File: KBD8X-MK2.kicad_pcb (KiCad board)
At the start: 2 copper layers, 343.7 x 118.3 mm, 347 parts, among them J1 AVR-ISP-6, Q1 DSS60601MZ4-13, SW1 SW_Push, SW2 SW_SPDT, SW3 SW_SPDT, U1 ATmega32U4-MU, U2 PRTR5V0U2X, Y1 16MHz

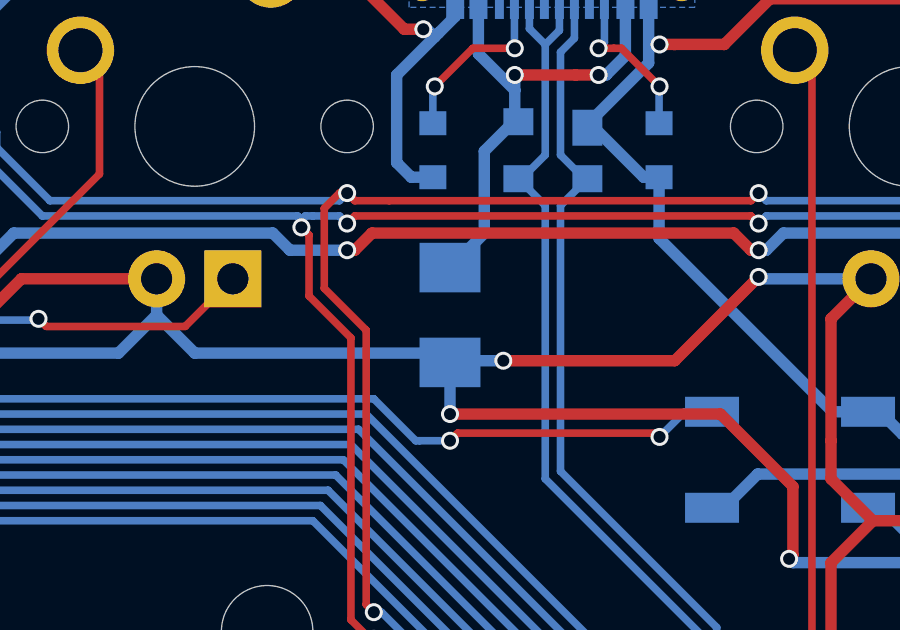
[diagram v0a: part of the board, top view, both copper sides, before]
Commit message: Made the project portable
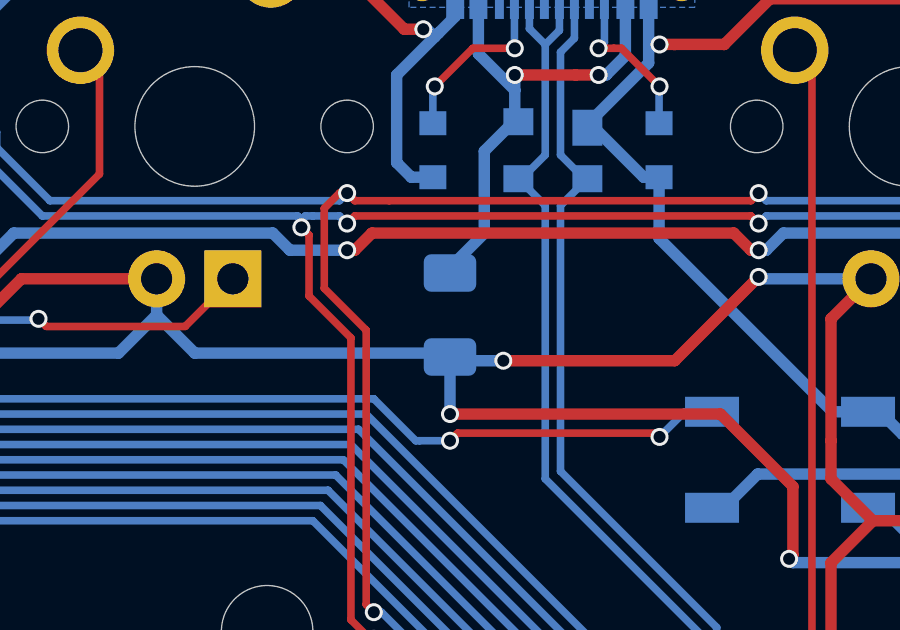
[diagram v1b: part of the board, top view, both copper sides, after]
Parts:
- C2, C3, C4, C5, C6, C7, C8, CRGB1, CRGB10, CRGB11, CRGB12, CRGB13, CRGB14, CRGB15, CRGB16, CRGB17, CRGB18, CRGB2, CRGB3, CRGB4, CRGB5, CRGB6, CRGB7, CRGB8, CRGB9: footprint locallib:C_0603 -> KBD8X_MK2_Components:C_0603
- D1, D10, D100, D101, D108, D11, D111, D112, D113, D12, D13, D14, D17, D18, D19, D2, D20, D21, D22, D23, D24, D25, D26, D27, D28, D29, D3, D30, D31, D35, D36, D37, D38, D39, D4, D40, D41, D42, D43, D44, D45, D46, D47, D48, D5, D52, D53, D54, D55, D56, D57, D58, D59, D6, D60, D61, D62, D63, D65, D66, D67, D68, D69, D7, D70, D71, D72, D73, D74, D75, D76, D77, D78, D8, D81, D82, D84, D85, D86, D87, D9, D90, D91, D92, D93, D94, D95, D96, D97, D99: footprint locallib:D_SOD-123 -> KBD8X_MK2_Components:D_SOD-123
- F1: footprint Fuse_Holders_and_Fuses:Fuse_SMD1206_Wave -> KBD8X_MK2_Components:Fuse_1206_3216Metric
- G***: footprint locallib:kbd8x-logo -> KBD8X_MK2_Graphics:kbd8x-logo
- G***: footprint locallib:ai-ring-6mm -> KBD8X_MK2_Graphics:ai-ring-6mm
- G***: footprint locallib:ai-ring-6mm-FancyAss-Mask -> KBD8X_MK2_Graphics:ai-ring-6mm-FancyAss-Mask
- G***: footprint locallib:ai-ring-6mm-FancyAss -> KBD8X_MK2_Graphics:ai-ring-6mm-FancyAss
- J1: footprint random-keyboard-parts:Reset_Pretty-Mask -> KBD8X_MK2_Components:Reset_Pretty-Mask
- MX_#0_1, MX_#1, MX_#2, MX_#3, MX_#4, MX_#5, MX_#6, MX_#7, MX_#8, MX_#9, MX_'1, MX_,1, MX_-1, MX_.1, MX_/1, MX_;1, MX_=1, MX_A1, MX_B1, MX_BACK2, MX_BACK3, MX_C1, MX_D1, MX_DEL1, MX_DN1, MX_E1, MX_END1, MX_ESC1, MX_F1, MX_FN1, MX_FN10, MX_FN11, MX_FN12, MX_FN2, MX_FN3, MX_FN4, MX_FN5, MX_FN6, MX_FN7, MX_FN8, MX_FN9, MX_G1, MX_H1, MX_HOME1, MX_I1, MX_INS1, MX_J1, MX_K1, MX_L1, MX_LFT1, MX_LSHIFT3, MX_M1, MX_N1, MX_O1, MX_P1, MX_PAUSE1, MX_PGDN1, MX_PGUP1, MX_PRINT1, MX_Q1, MX_R1, MX_RGUI2, MX_RSHIFT3, MX_RT1, MX_S1, MX_SLOCK1, MX_T1, MX_U1, MX_UP1, MX_V1, MX_W1, MX_X1, MX_Y1, MX_Z1, MX_[1, MX_\2, MX_]1, MX_`1: footprint MX_Alps_Hybrid:MXOnly-1U -> KBD8X_MK2_Switches:MXOnly-1U
- MX_BACK1: footprint MX_Alps_Hybrid:MXOnly-2U -> KBD8X_MK2_Switches:MXOnly-2U
- MX_CLOCK1, MX_RSHIFT2: footprint MX_Alps_Hybrid:MXOnly-1.75U -> KBD8X_MK2_Switches:MXOnly-1.75U
- MX_CLOCK2, MX_RCTRL1, MX_RGUI1, MX_RMENU1: footprint MX_Alps_Hybrid:MXOnly-1.25U-FLIPPED -> KBD8X_MK2_Switches:MXOnly-1.25U-FLIPPED
- MX_LALT1, MX_LCTRL1, MX_LGUI1, MX_LSHIFT2, MX_RALT1: footprint MX_Alps_Hybrid:MXOnly-1.25U -> KBD8X_MK2_Switches:MXOnly-1.25U
- MX_LALT2, MX_LCTRL2: footprint MX_Alps_Hybrid:MXOnly-1.5U-FLIPPED -> KBD8X_MK2_Switches:MXOnly-1.5U-FLIPPED
- MX_LGUI2: footprint MX_Alps_Hybrid:MXOnly-1U-FLIPPED -> KBD8X_MK2_Switches:MXOnly-1U-FLIPPED
- MX_LSHIFT1, MX_RETURN1: footprint MX_Alps_Hybrid:MXOnly-2.25U -> KBD8X_MK2_Switches:MXOnly-2.25U
- MX_RALT2, MX_RCTRL2, MX_TAB1, MX_\1: footprint MX_Alps_Hybrid:MXOnly-1.5U -> KBD8X_MK2_Switches:MXOnly-1.5U
- MX_RETURN2: footprint MX_Alps_Hybrid:MXOnly-ISO-ROTATED-ReversedStabilizers -> KBD8X_MK2_Switches:MXOnly-ISO-ROTATED-ReversedStabilizers
- MX_RSHIFT1: footprint MX_Alps_Hybrid:MXOnly-2.75U -> KBD8X_MK2_Switches:MXOnly-2.75U
- MX_SP1: footprint MX_Alps_Hybrid:MXOnly-6.25U-ReversedStabilizers -> KBD8X_MK2_Switches:MXOnly-6.25U-ReversedStabilizers
- MX_SP2: footprint MX_Alps_Hybrid:MXOnly-7U-ReversedStabilizers -> KBD8X_MK2_Switches:MXOnly-7U-ReversedStabilizers
- Q1: footprint TO_SOT_Packages_SMD:SOT-223-3_TabPin2 -> KBD8X_MK2_Components:SOT-223-3_TabPin2
- R1, R10, R100, R101, R108, R11, R111, R112, R113, R12, R13, R14, R16, R17, R18, R19, R2, R20, R21, R22, R23, R24, R25, R26, R27, R28, R29, R3, R30, R31, R32, R33, R35, R36, R37, R38, R39, R4, R40, R41, R42, R43, R44, R45, R46, R47, R48, R5, R52, R53, R54, R55, R56, R57, R58, R59, R6, R60, R61, R62, R63, R65, R66, R67, R68, R69, R7, R70, R71, R72, R73, R74, R75, R76, R77, R78, R8, R81, R82, R84, R85, R86, R87, R9, R90, R91, R95, R96, R97, R99, RC1, RC2, RC3, RC4, RC5, RC6, RC7: footprint locallib:R_0603 -> KBD8X_MK2_Components:R_0603
- RGB1, RGB10, RGB11, RGB12, RGB13, RGB14, RGB15, RGB16, RGB17, RGB18, RGB2, RGB3, RGB4, RGB5, RGB6, RGB7, RGB8, RGB9: footprint locallib:LED_WS2812B-PLCC4 -> KBD8X_MK2_Components:LED_WS2812B-PLCC4
- SW1: footprint random-keyboard-parts:SKQG-1155865 -> KBD8X_MK2_Components:SKQG-1155865
- SW2, SW3: footprint Buttons_Switches_SMD:SW_SPDT_PCM12 -> KBD8X_MK2_Components:SW_SPDT_PCM12
- U1: footprint locallib:QFN-44-1EP_7x7mm_Pitch0.5mm -> KBD8X_MK2_Components:QFN-44-1EP_7x7mm_Pitch0.5mm
- U2: footprint locallib:SOT143B -> KBD8X_MK2_Components:SOT143B
- USB1: footprint Type-C:HRO-TYPE-C-31-M-12-Assembly -> KBD8X_MK2_Components:HRO-TYPE-C-31-M-12-Assembly
- Y1: footprint locallib:Crystal_SMD_3225-4pin_3.2x2.5mm -> KBD8X_MK2_Components:Crystal_SMD_3225-4pin_3.2x2.5mm

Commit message: Rearrenged schematics items
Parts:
- removed G***: LOGO, KBD8X_MK2_Graphics:kbd8x-logo
- removed G***: LOGO, KBD8X_MK2_Graphics:ai-ring-6mm
- removed G***: LOGO, KBD8X_MK2_Graphics:ai-ring-6mm-FancyAss-Mask
- removed G***: LOGO, KBD8X_MK2_Graphics:ai-ring-6mm-FancyAss
- added H1: KBD8X-MKII Logo, KBD8X_MK2_Graphics:kbd8x-logo, F.Cu at (231.2, 252.9)
- added H2: ai03 logo, KBD8X_MK2_Graphics:ai-ring-6mm-FancyAss, B.Cu at (303.2, 252.4)
- added H3: ai03 logo, KBD8X_MK2_Graphics:ai-ring-6mm-FancyAss-Mask, B.Cu at (303.2, 252.4)
- added H4: ai03 logo, KBD8X_MK2_Graphics:ai-ring-6mm, F.Cu at (315.2, 253.2)
- D1, D10, D100, D101, D108, D11, D111, D112, D113, D12, D13, D14, D17, D18, D19, D2, D20, D21, D22, D23, D24, D25, D26, D27, D28, D29, D3, D30, D31, D35, D36, D37, D38, D39, D4, D40, D41, D42, D43, D44, D45, D46, D47, D48, D5, D52, D53, D54, D55, D56, D57, D58, D59, D6, D60, D61, D62, D63, D65, D66, D67, D68, D69, D7, D70, D71, D72, D73, D74, D75, D76, D77, D78, D8, D81, D82, D84, D85, D86, D87, D9, D90, D91, D92, D93, D94, D95, D96, D97, D99: value SOD-323 -> SOD-123
- RGB1, RGB10, RGB11, RGB12, RGB13, RGB14, RGB15, RGB16, RGB17, RGB18, RGB2, RGB3, RGB4, RGB5, RGB6, RGB7, RGB8, RGB9: footprint KBD8X_MK2_Components:LED_WS2812B-PLCC4 -> LED_SMD:LED_WS2812B_PLCC4_5.0x5.0mm_P3.2mm
- U1: footprint KBD8X_MK2_Components:QFN-44-1EP_7x7mm_Pitch0.5mm -> Package_DFN_QFN:QFN-44-1EP_7x7mm_P0.5mm_EP5.2x5.2mm
- moved CRGB10 144.0 mm to (146.1, 252.4)
- moved CRGB12 144.0 mm to (241.3, 252.4)
- moved CRGB13 144.0 mm to (281.8, 252.4)
- moved CRGB14 144.0 mm to (312.8, 252.4)
- moved CRGB16 144.0 mm to (412.8, 252.4)
- moved CRGB17 144.0 mm to (446.9, 254.8)
- moved D100 144.0 mm to (451.7, 196.9)
- moved D101 144.0 mm to (454.9, 196.9)
- moved D37 144.0 mm to (189.7, 196.9)
- moved D39 144.0 mm to (227.8, 196.9)
- moved D40 144.0 mm to (246.9, 196.9)
- moved D41 144.0 mm to (265.9, 196.9)
- moved D42 144.0 mm to (285.0, 196.9)
- moved D43 144.0 mm to (304.0, 196.9)
- moved D46 144.0 mm to (361.2, 196.9)
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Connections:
- RGB18 pad 2: Net-(RGB18-Pad2) -> unconnected-(RGB18-Pad2)
- SW1 pad 3: (no net) -> unconnected-(SW1-Pad3)
- SW1 pad 4: (no net) -> unconnected-(SW1-Pad4)
- U1 pad 42: Net-(U1-Pad42) -> unconnected-(U1-Pad42)
- USB1 pad 3: Net-(USB1-Pad3) -> unconnected-(USB1-Pad3)
- USB1 pad 9: Net-(USB1-Pad9) -> unconnected-(USB1-Pad9)
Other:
- outline, holes or cut-outs redrawn

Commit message: Updated symbols used in the schematics
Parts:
- MX_#0_1, MX_#1, MX_#2, MX_#3, MX_#4, MX_#5, MX_#6, MX_#7, MX_#8, MX_#9, MX_'1, MX_,1, MX_-1, MX_.1, MX_/1, MX_;1, MX_=1, MX_A1, MX_B1, MX_BACK2, MX_BACK3, MX_C1, MX_D1, MX_DEL1, MX_DN1, MX_E1, MX_END1, MX_ESC1, MX_F1, MX_FN1, MX_FN10, MX_FN11, MX_FN12, MX_FN2, MX_FN3, MX_FN4, MX_FN5, MX_FN6, MX_FN7, MX_FN8, MX_FN9, MX_G1, MX_H1, MX_HOME1, MX_I1, MX_INS1, MX_J1, MX_K1, MX_L1, MX_LFT1, MX_LGUI2, MX_LSHIFT3, MX_M1, MX_N1, MX_O1, MX_P1, MX_PAUSE1, MX_PGDN1, MX_PGUP1, MX_PRINT1, MX_Q1, MX_R1, MX_RGUI2, MX_RSHIFT3, MX_RT1, MX_S1, MX_SLOCK1, MX_T1, MX_U1, MX_UP1, MX_V1, MX_W1, MX_X1, MX_Y1, MX_Z1, MX_[1, MX_\2, MX_]1, MX_`1: value MX-1U -> MX-LED
- MX_BACK1: value MX-2U -> MX-LED
- MX_CLOCK1, MX_RSHIFT2: value MX-1.75U -> MX-LED
- MX_CLOCK2, MX_LALT1, MX_LCTRL1, MX_LGUI1, MX_LSHIFT2, MX_RALT1, MX_RCTRL1, MX_RGUI1, MX_RMENU1: value MX-1.25U -> MX-LED
- MX_LALT2, MX_LCTRL2, MX_RALT2, MX_RCTRL2, MX_TAB1, MX_\1: value MX-1.5U -> MX-LED
- MX_LSHIFT1, MX_RETURN1: value MX-2.25U -> MX-LED
- MX_RETURN2: value MX-ISO -> MX-LED
- MX_RSHIFT1: value MX-2.75U -> MX-LED
- MX_SP1: value MX-6.25U -> MX-LED
- MX_SP2: value MX-7U -> MX-LED

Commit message: Removed leds and unnecessary resistors
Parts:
- removed Q1: DSS60601MZ4-13, KBD8X_MK2_Components:SOT-223-3_TabPin2
- removed R1, R10, R100, R101, R108, R11, R111, R112, R113, R12, R13, R14, R16, R17, R18, R19, R2, R20, R21, R22, R23, R24, R25, R26, R27, R28, R29, R3, R30, R31, R33, R35, R36, R37, R38, R39, R4, R40, R41, R42, R43, R44, R45, R46, R47, R48, R5, R53, R54, R55, R56, R57, R58, R59, R6, R60, R61, R62, R63, R65, R66, R67, R68, R69, R7, R70, R71, R72, R73, R74, R75, R76, R77, R78, R8, R81, R82, R84, R85, R86, R87, R9, R90, R91, R95, R96, R97, R99: 1k, KBD8X_MK2_Components:R_0603
- removed RC5: 1.5k, KBD8X_MK2_Components:R_0603
- removed SW2, SW3: SW_SPDT, KBD8X_MK2_Components:SW_SPDT_PCM12
- MX_#0_1, MX_#1, MX_#2, MX_#3, MX_#4, MX_#5, MX_#6, MX_#7, MX_#8, MX_#9, MX_'1, MX_,1, MX_-1, MX_.1, MX_/1, MX_;1, MX_=1, MX_A1, MX_B1, MX_BACK2, MX_BACK3, MX_C1, MX_D1, MX_DEL1, MX_DN1, MX_E1, MX_END1, MX_ESC1, MX_F1, MX_FN1, MX_FN10, MX_FN11, MX_FN12, MX_FN2, MX_FN3, MX_FN4, MX_FN5, MX_FN6, MX_FN7, MX_FN8, MX_FN9, MX_G1, MX_H1, MX_HOME1, MX_I1, MX_INS1, MX_J1, MX_K1, MX_L1, MX_LFT1, MX_LSHIFT3, MX_M1, MX_N1, MX_O1, MX_P1, MX_PAUSE1, MX_PGDN1, MX_PGUP1, MX_PRINT1, MX_Q1, MX_R1, MX_RGUI2, MX_RSHIFT3, MX_RT1, MX_S1, MX_T1, MX_U1, MX_UP1, MX_V1, MX_W1, MX_X1, MX_Y1, MX_Z1, MX_[1, MX_\2, MX_]1, MX_`1: value MX-LED -> MX-NoLED; footprint KBD8X_MK2_Switches:MXOnly-1U -> KBD8X_MK2_Switches:MXOnly-1U-NoLED
- MX_BACK1: value MX-LED -> MX-NoLED; footprint KBD8X_MK2_Switches:MXOnly-2U -> KBD8X_MK2_Switches:MXOnly-2U-NoLED
- MX_LALT1, MX_LCTRL1, MX_LGUI1, MX_LSHIFT2, MX_RALT1: value MX-LED -> MX-NoLED; footprint KBD8X_MK2_Switches:MXOnly-1.25U -> KBD8X_MK2_Switches:MXOnly-1.25U-NoLED
- MX_LALT2, MX_LCTRL2: value MX-LED -> MX-NoLED; footprint KBD8X_MK2_Switches:MXOnly-1.5U-FLIPPED -> KBD8X_MK2_Switches:MXOnly-1.5U-NoLED
- MX_LGUI2: value MX-LED -> MX-NoLED; footprint KBD8X_MK2_Switches:MXOnly-1U-FLIPPED -> KBD8X_MK2_Switches:MXOnly-1U-NoLED
- MX_LSHIFT1, MX_RETURN1: value MX-LED -> MX-NoLED; footprint KBD8X_MK2_Switches:MXOnly-2.25U -> KBD8X_MK2_Switches:MXOnly-2.25U-NoLED
- MX_RALT2, MX_RCTRL2, MX_TAB1, MX_\1: value MX-LED -> MX-NoLED; footprint KBD8X_MK2_Switches:MXOnly-1.5U -> KBD8X_MK2_Switches:MXOnly-1.5U-NoLED
- MX_RCTRL1, MX_RGUI1, MX_RMENU1: value MX-LED -> MX-NoLED; footprint KBD8X_MK2_Switches:MXOnly-1.25U-FLIPPED -> KBD8X_MK2_Switches:MXOnly-1.25U-NoLED
- MX_RETURN2: value MX-LED -> MX-NoLED; footprint KBD8X_MK2_Switches:MXOnly-ISO-ROTATED-ReversedStabilizers -> KBD8X_MK2_Switches:MXOnly-ISO-ROTATED-ReversedStabilizers-NoLED
- MX_RSHIFT1: value MX-LED -> MX-NoLED; footprint KBD8X_MK2_Switches:MXOnly-2.75U -> KBD8X_MK2_Switches:MXOnly-2.75U-NoLED
- MX_RSHIFT2: value MX-LED -> MX-NoLED; footprint KBD8X_MK2_Switches:MXOnly-1.75U -> KBD8X_MK2_Switches:MXOnly-1.75U-NoLED
- MX_SP1: value MX-LED -> MX-NoLED; footprint KBD8X_MK2_Switches:MXOnly-6.25U-ReversedStabilizers -> KBD8X_MK2_Switches:MXOnly-6.25U-ReversedStabilizers-NoLED
- MX_SP2: value MX-LED -> MX-NoLED; footprint KBD8X_MK2_Switches:MXOnly-7U-ReversedStabilizers -> KBD8X_MK2_Switches:MXOnly-7U-ReversedStabilizers-NoLED
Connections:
- net CAPS_LEDGND renamed Net-(MX_CLOCK1-Pad4)
- net SLOCK_LEDGND renamed Net-(MX_SLOCK1-Pad4)
- R32 pad 1: Net-(R32-Pad1) -> SLOCK_IND
- R52 pad 2: Net-(R52-Pad2) -> CAPS_IND
- U1 pad 12: Net-(RC5-Pad1) -> unconnected-(U1-Pad12)
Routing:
- net LEDGND: track 1914.1 -> 0.00 mm, vias 15 -> 0
- net +5V: track 2658.4 -> 1082.5 mm
- net Net-(MX_RETURN1-Pad4): track 42.9 -> 0.00 mm
- net Net-(MX_LSHIFT1-Pad4): track 36.8 -> 0.00 mm
- net Net-(MX_\1-Pad4): track 36.4 -> 0.00 mm, vias 1 -> 0
- net Net-(MX_BACK3-Pad4): track 36.1 -> 0.00 mm
- net Net-(RC5-Pad1): track 31.4 -> 0.00 mm
- net Net-(MX_PGDN1-Pad4): track 30.5 -> 0.00 mm
- net Net-(MX_BACK1-Pad4): track 26.3 -> 0.00 mm
- net Net-(MX_SP1-Pad4): track 23.4 -> 0.00 mm
- net Net-(MX_RSHIFT1-Pad4): track 18.0 -> 0.00 mm
- net Net-(MX_PAUSE1-Pad4): track 11.4 -> 0.00 mm, vias 2 -> 0
- net Net-(MX_PGUP1-Pad4): track 11.0 -> 0.00 mm
- net Net-(MX_LALT1-Pad4): track 10.2 -> 0.00 mm
- net Net-(MX_RT1-Pad4): track 10.2 -> 0.00 mm
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
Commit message: Removed everything related to RGB
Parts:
- removed CRGB1, CRGB10, CRGB11, CRGB12, CRGB13, CRGB14, CRGB15, CRGB16, CRGB17, CRGB18, CRGB2, CRGB3, CRGB4, CRGB5, CRGB6, CRGB7, CRGB8, CRGB9: 0.1uF, KBD8X_MK2_Components:C_0603
- removed RGB1, RGB10, RGB11, RGB12, RGB13, RGB14, RGB15, RGB16, RGB17, RGB18, RGB2, RGB3, RGB4, RGB5, RGB6, RGB7, RGB8, RGB9: WS2812B, LED_SMD:LED_WS2812B_PLCC4_5.0x5.0mm_P3.2mm
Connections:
- net RGBLED renamed MISO
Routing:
- net GND: track 1182.3 -> 206.8 mm, vias 17 -> 3
- net +5V: track 1082.5 -> 524.8 mm, vias 34 -> 11
- net Net-(RGB8-Pad2): track 66.6 -> 0.00 mm, vias 2 -> 0
- net MISO: track 103.4 -> 42.8 mm, vias 2 -> 0
- net Net-(RGB2-Pad2): track 60.4 -> 0.00 mm, vias 4 -> 0
- net Net-(RGB10-Pad4): track 57.7 -> 0.00 mm, vias 2 -> 0
- net Net-(RGB7-Pad2): track 55.6 -> 0.00 mm
- net Net-(RGB17-Pad2): track 54.9 -> 0.00 mm, vias 2 -> 0
- net Net-(RGB16-Pad2): track 53.0 -> 0.00 mm, vias 2 -> 0
- net Net-(RGB3-Pad2): track 51.6 -> 0.00 mm
- net Net-(RGB5-Pad2): track 51.6 -> 0.00 mm
- net Net-(RGB6-Pad2): track 50.0 -> 0.00 mm
- net Net-(RGB4-Pad2): track 50.0 -> 0.00 mm
- net Net-(RGB10-Pad2): track 47.6 -> 0.00 mm
- net Net-(RGB15-Pad2): track 47.2 -> 0.00 mm
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
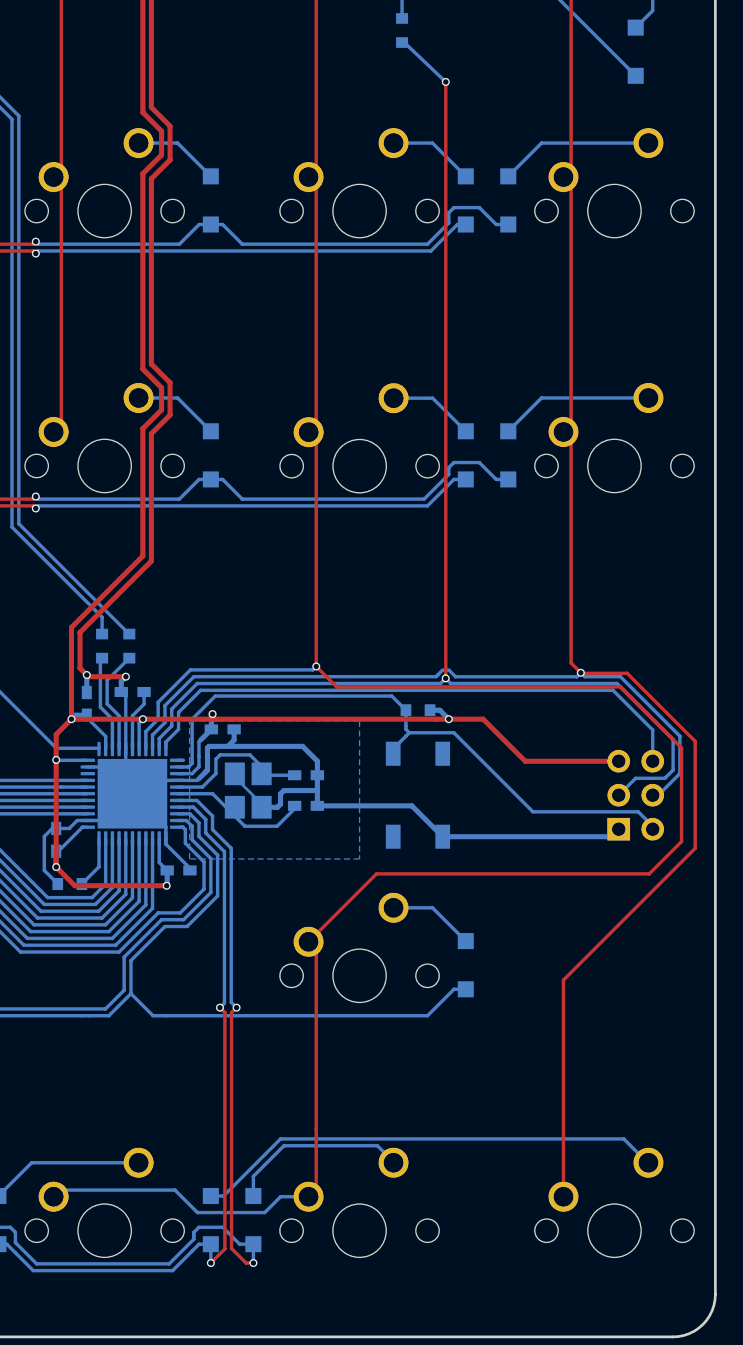
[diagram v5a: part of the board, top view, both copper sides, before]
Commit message: Added OLED display
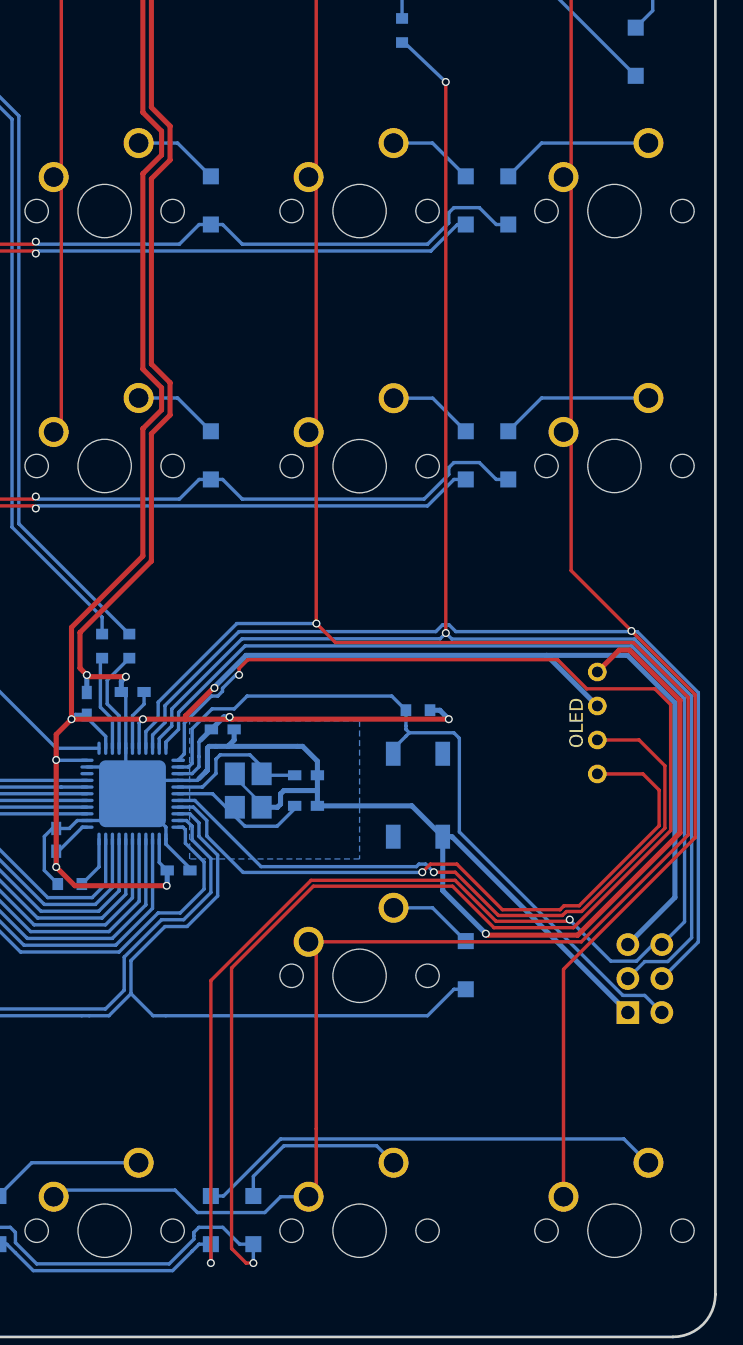
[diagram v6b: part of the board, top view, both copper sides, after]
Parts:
- added OL1: OLED, KBD8X_MK2_Components:OLED, F.Cu at (461.5, 216.9)
- U1: footprint Package_DFN_QFN:QFN-44-1EP_7x7mm_P0.5mm_EP5.2x5.2mm -> KBD8X_MK2_Components:QFN-44-1EP_7x7mm_Pitch0.5mm
- moved J1 13.7 mm to (465.1, 236.0)
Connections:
- J1 pad 1: MISO -> ROW10
- U1 pad 11: MISO -> ROW10
- U1 pad 12: unconnected-(U1-Pad12) -> ROW11
- U1 pad 18: ROW11 -> SCL
- U1 pad 19: ROW10 -> SDA
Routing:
- net ROW10: track 306.1 -> 393.7 mm
- net ROW11: track 321.3 -> 398.6 mm
- net SCL: track 0.00 -> 53.3 mm, vias 0 -> 1
- net +5V: track 524.8 -> 576.3 mm, vias 11 -> 12
- net SDA: track 0.00 -> 50.7 mm, vias 0 -> 1
- net GND: track 206.8 -> 257.3 mm, vias 3 -> 4
- net MISO: track 42.8 -> 0.00 mm
- net COL8: track 162.1 -> 179.7 mm
- net SLOCK_IND: track 99.8 -> 116.2 mm
- net RESET: track 46.8 -> 56.7 mm
- net COL7: track 250.5 -> 252.8 mm
